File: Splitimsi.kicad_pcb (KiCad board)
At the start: 2 copper layers, 118.2 x 99.3 mm, 30 parts, among them SW1 MX_RGB, SW10 MX_RGB, SW11 MX_RGB, SW12 MX_RGB, SW13 MX_RGB, SW14 MX_RGB, SW15 MX_RGB, SW16 MX_RGB, SW17 MX_RGB, SW18 MX_RGB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

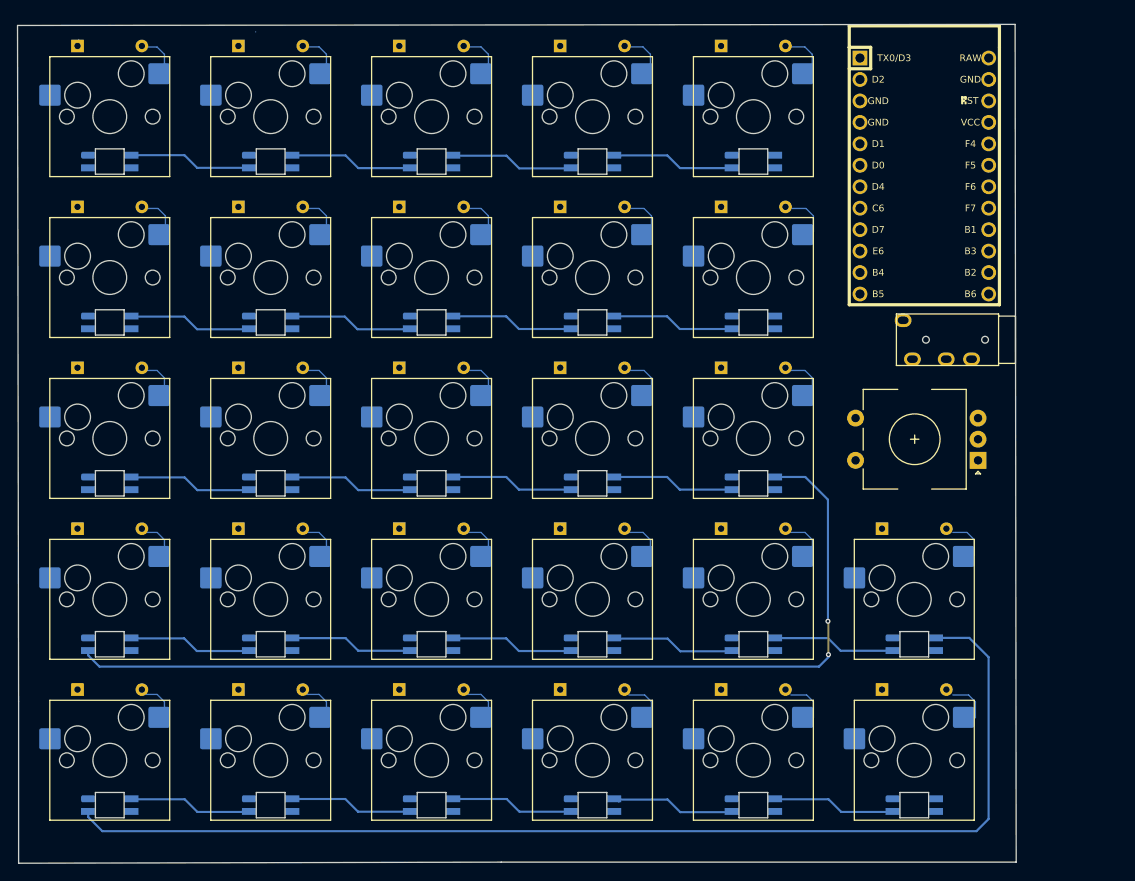
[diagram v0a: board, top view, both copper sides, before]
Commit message: tht diode footprints changed with smds
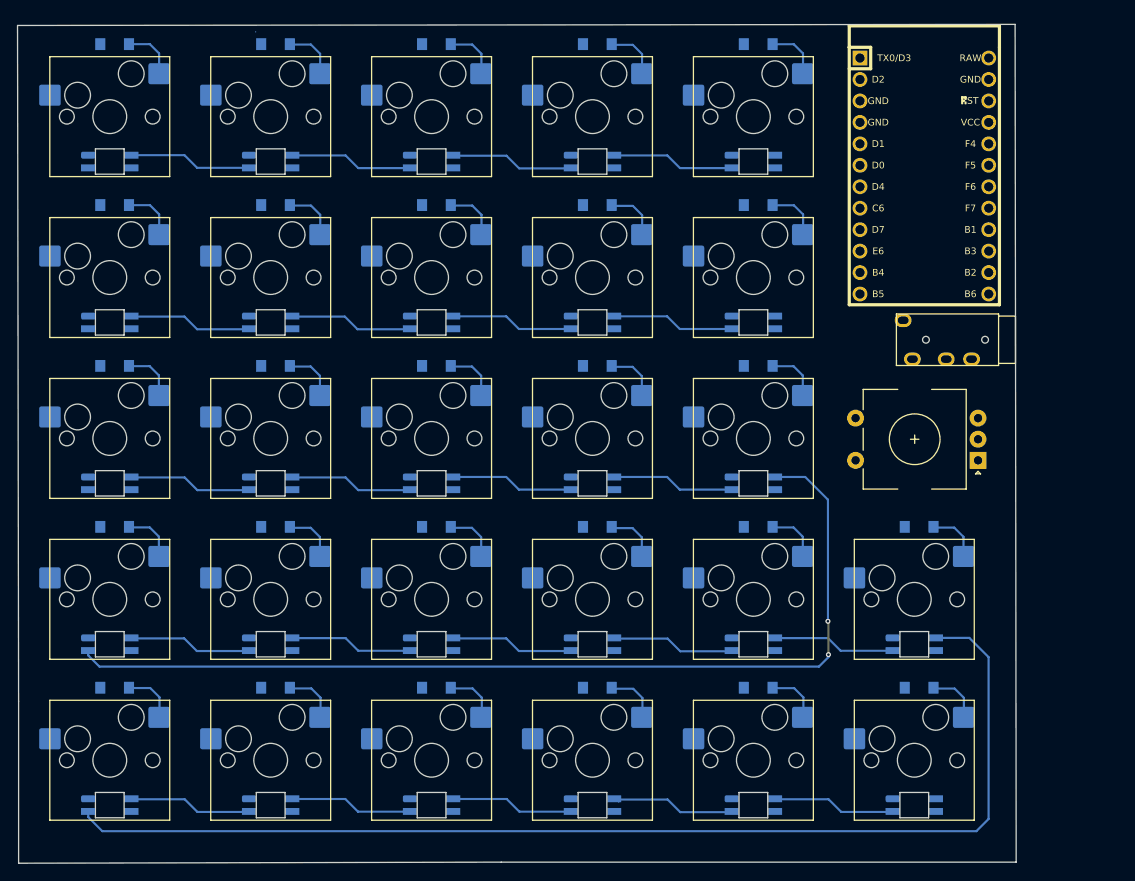
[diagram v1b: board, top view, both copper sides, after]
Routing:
- net /Row0: track 1.83 -> 0.01 mm
- net Net-(SW14-Pad2): track 4.82 -> 6.43 mm
- net Net-(SW12-Pad2): track 4.82 -> 6.43 mm
- net Net-(SW11-Pad2): track 4.82 -> 6.43 mm
- net Net-(SW9-Pad2): track 4.82 -> 6.43 mm
- net Net-(SW17-Pad2): track 4.82 -> 6.43 mm
- net Net-(SW16-Pad2): track 4.82 -> 6.43 mm
- net Net-(SW15-Pad2): track 4.82 -> 6.43 mm
- net Net-(SW20-Pad2): track 4.82 -> 6.43 mm
- net Net-(SW6-Pad2): track 4.82 -> 6.43 mm
- net Net-(SW4-Pad2): track 4.82 -> 6.43 mm
- net Net-(SW1-Pad2): track 5.54 -> 7.15 mm
- net Net-(SW7-Pad2): track 4.82 -> 6.43 mm
- net Net-(SW10-Pad2): track 4.82 -> 6.43 mm
- net Net-(SW5-Pad2): track 4.82 -> 6.43 mm
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
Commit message: Row tracks connected to the Mcu
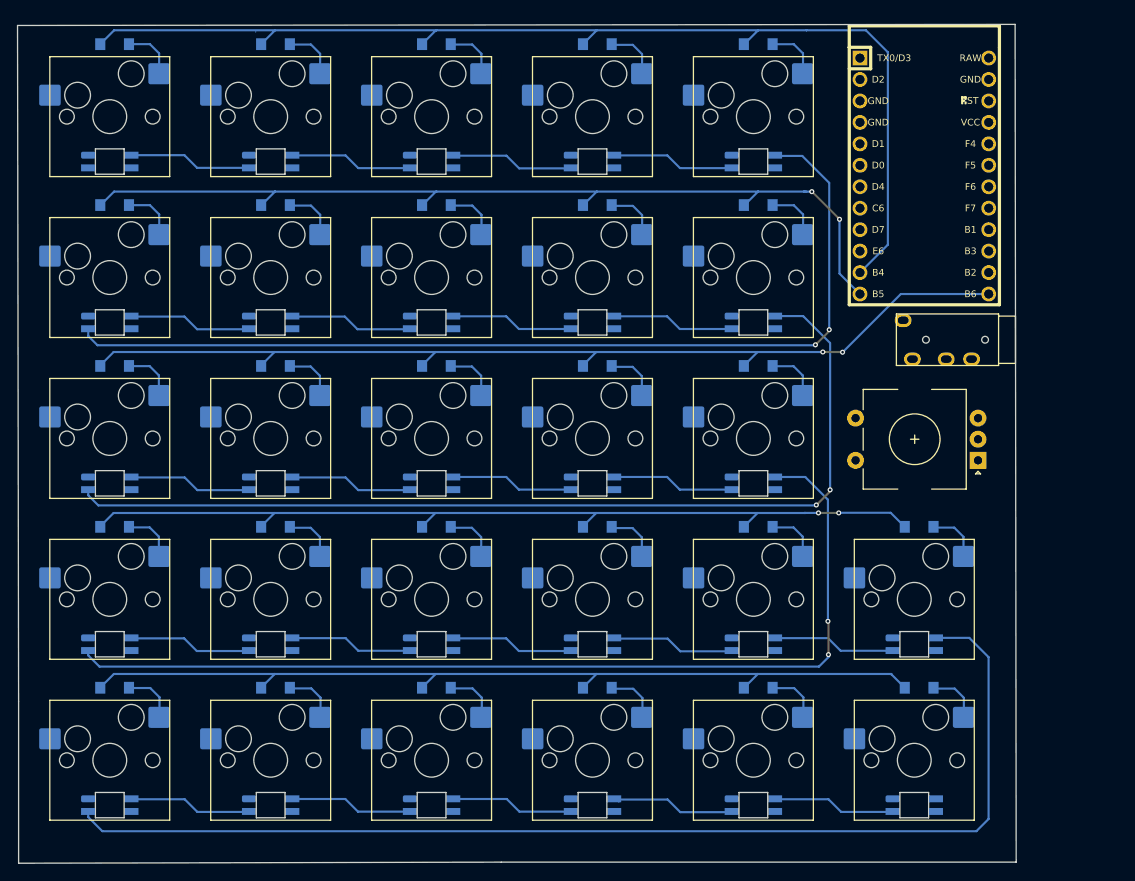
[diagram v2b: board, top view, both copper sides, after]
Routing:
- net /Row0: track 0.01 -> 131.9 mm
- net /Row2: track 0.00 -> 118.1 mm, vias 0 -> 2
- net /Row1_LedOut: track 0.00 -> 115.1 mm, vias 0 -> 2
- net /Row0_LedOut: track 0.00 -> 114.8 mm, vias 0 -> 2
- net /Row1: track 0.00 -> 109.0 mm, vias 0 -> 2
- net /Row3: track 0.00 -> 106.1 mm, vias 0 -> 2
- net /Row4: track 0.00 -> 105.9 mm

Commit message: v0.5
- rows and columns connected to the MCU
- main tracks connected except rst button, knob, gnd, trrs
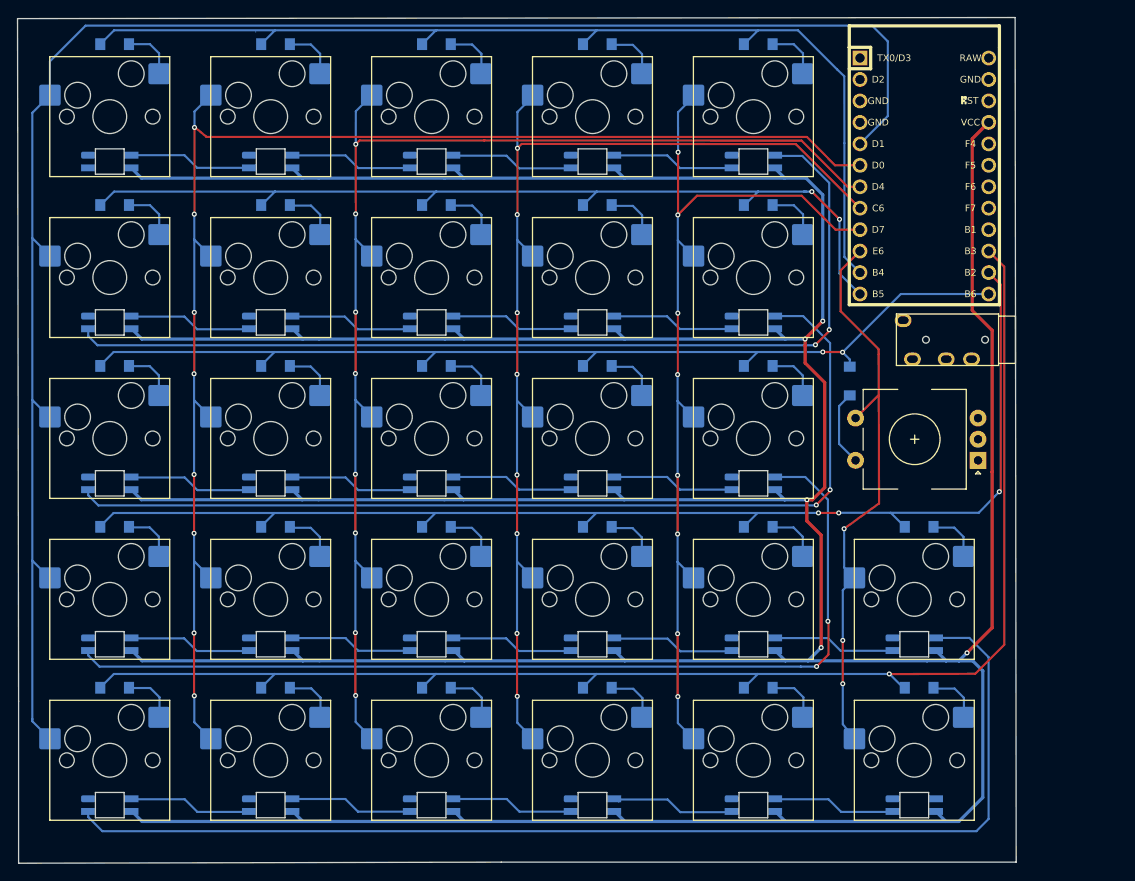
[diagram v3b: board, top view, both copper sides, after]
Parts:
- added D1: DIODE, Keebio-Parts:D_SOD123, B.Cu at (118.7, 59.9)
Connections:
- Knob1 pad S2: unconnected-(Knob1-PadS2) -> Net-(D1-Pad1)
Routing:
- net +5V: track 0.00 -> 626.6 mm, vias 0 -> 5
- net /Col0: track 0.00 -> 206.0 mm
- net /Col1: track 0.00 -> 166.7 mm, vias 0 -> 8
- net /Col2: track 0.00 -> 148.3 mm, vias 0 -> 8
- net /Col3: track 0.00 -> 130.0 mm, vias 0 -> 8
- net /Col4: track 0.00 -> 110.3 mm, vias 0 -> 8
- net /Col5: track 0.00 -> 68.0 mm, vias 0 -> 3
- net /Row4: track 105.9 -> 168.4 mm, vias 0 -> 1
- net /Row3: track 106.1 -> 146.7 mm, vias 2 -> 3
- net Net-(D1-Pad1): track 0.00 -> 9.02 mm
- net /Row0: track 131.9 -> 124.4 mm
- net /Row2: track 118.1 -> 120.1 mm
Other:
- board size 118.2 x 99.3 mm -> 118.2 x 100.1 mm

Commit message: fucked up update
- ic2 resistors added
- trrs tracks connected to the mcu
- pin 5 and 6 deleted for column tracks
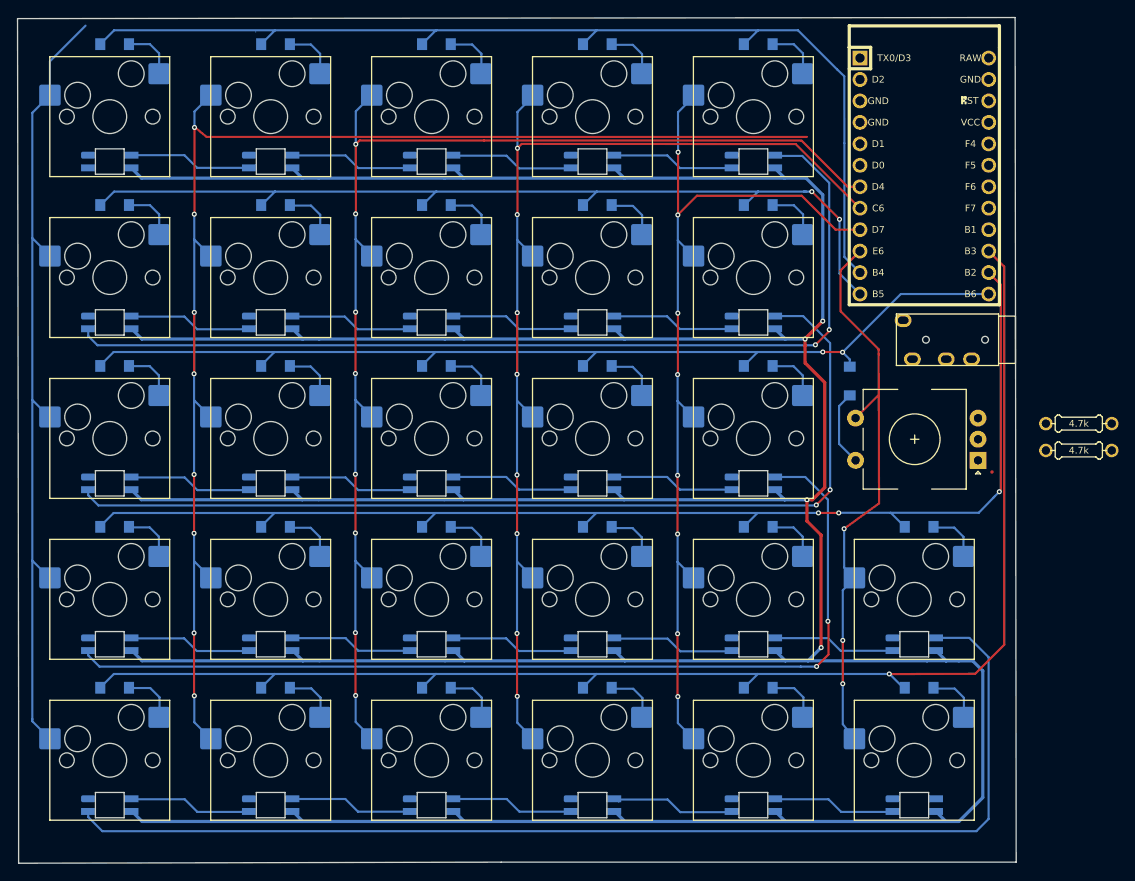
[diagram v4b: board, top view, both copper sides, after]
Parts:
- added R1: 4.7k, Keebio-Parts:Resistor-Compact-1-side, F.Cu at (145.8, 64.9)
- added R2: 4.7k, Keebio-Parts:Resistor-Compact-1-side, F.Cu at (145.8, 68.1)
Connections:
- SW1 pad 6: unconnected-(SW1-Pad6) -> /LedData
- U1 pad 1: unconnected-(U1-Pad1) -> /LedData
- U1 pad 5: /Col0 -> /SDA
- U1 pad 6: /Col1 -> /SCL
- U2 pad 1: unconnected-(U2-Pad1) -> +5V
- U2 pad 2: unconnected-(U2-Pad2) -> /SCL
- U2 pad 3: unconnected-(U2-Pad3) -> /SDA
- U2 pad 4: unconnected-(U2-Pad4) -> GND
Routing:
- net /Col0: track 206.0 -> 96.7 mm
- net +5V: track 626.6 -> 559.4 mm, vias 5 -> 4
- net /Col1: track 166.7 -> 159.1 mm

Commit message: TRRS resistors and footprints connected
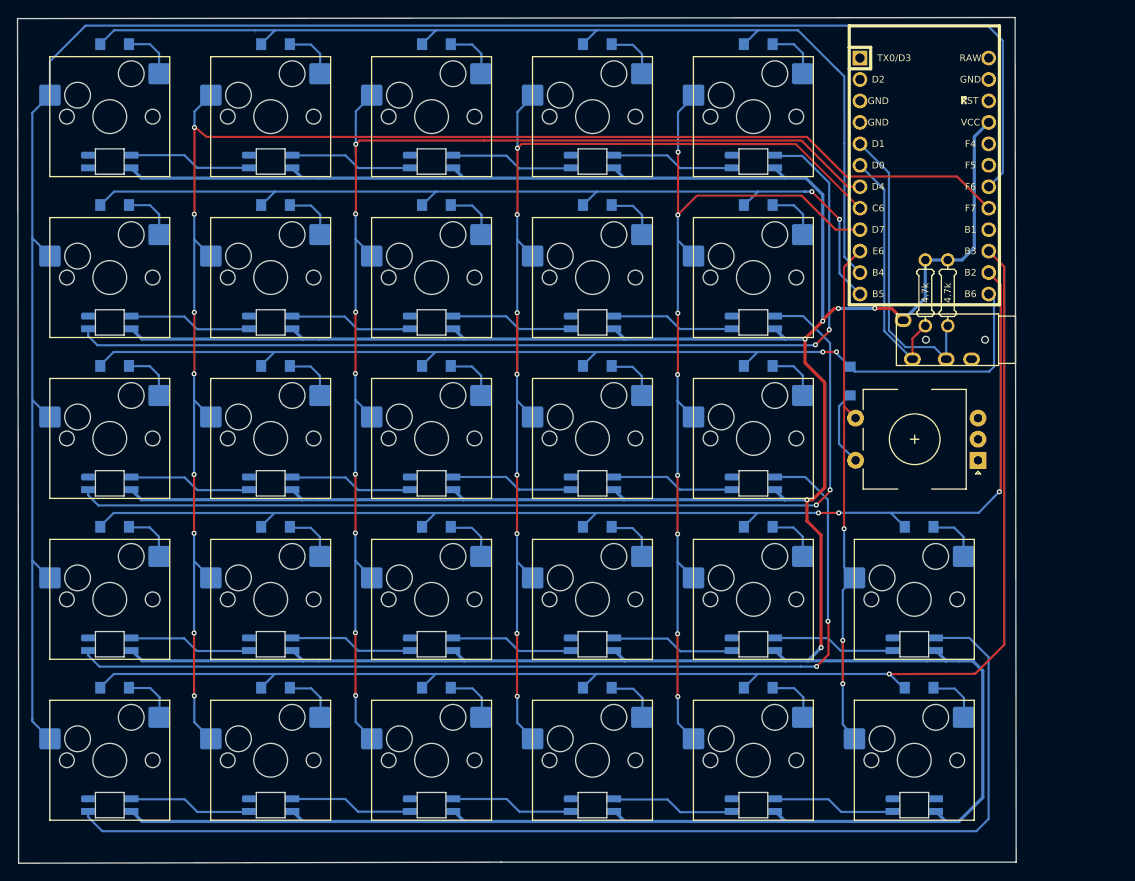
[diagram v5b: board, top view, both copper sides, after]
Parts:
- moved R2 26.0 mm to (127.7, 49.4), turned to 90 degrees
- moved R1 21.9 mm to (130.3, 49.4), turned to 90 degrees
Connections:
- U1 pad 17: unconnected-(U1-Pad17) -> /Col1
- U1 pad 18: unconnected-(U1-Pad18) -> /Col0
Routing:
- net /Col0: track 96.7 -> 224.0 mm
- net +5V: track 559.4 -> 600.4 mm, vias 4 -> 6
- net /SDA: track 0.00 -> 35.7 mm
- net /SCL: track 0.00 -> 30.1 mm
- net /Col1: track 159.1 -> 184.1 mm
- net /Col5: track 68.0 -> 62.0 mm
- net /Row2: track 120.1 -> 126.0 mm

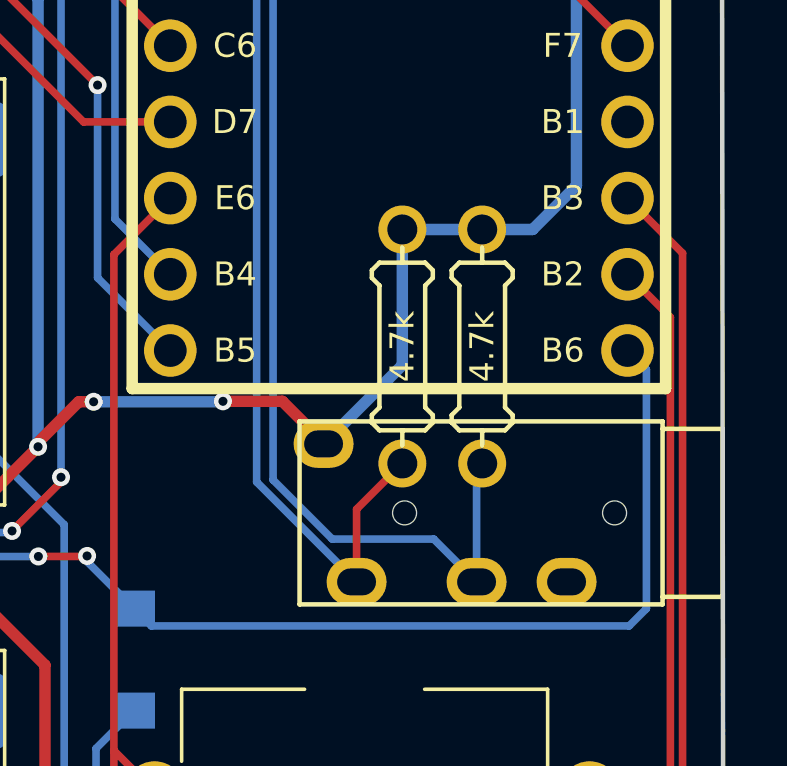
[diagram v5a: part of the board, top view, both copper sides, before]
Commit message: Resistor footprints changed with 1206
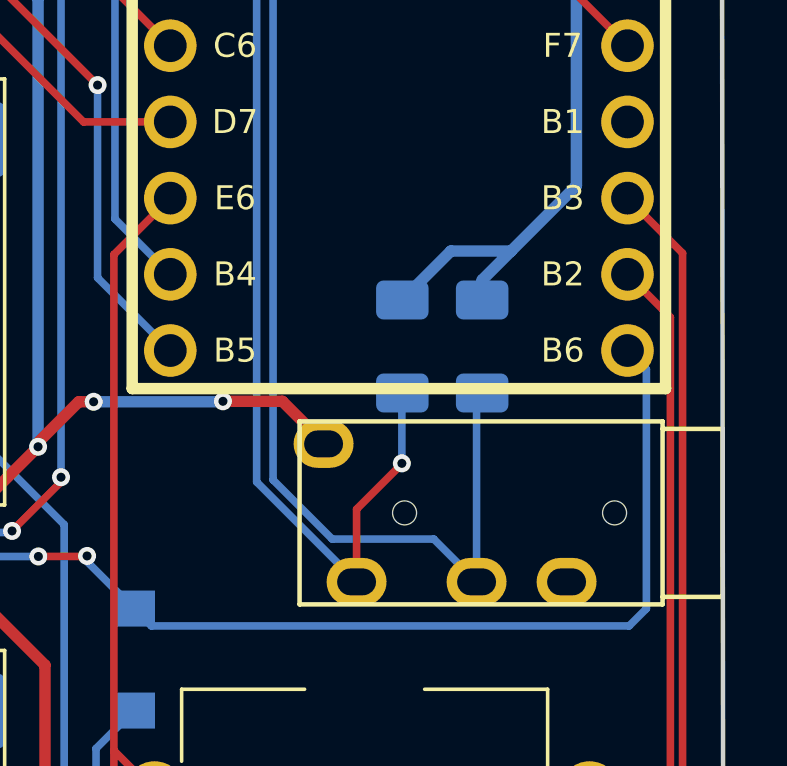
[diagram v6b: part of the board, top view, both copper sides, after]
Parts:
- R1, R2: footprint Keebio-Parts:Resistor-Compact-1-side -> Resistor_SMD:R_1206_3216Metric_Pad1.30x1.75mm_HandSolder; moved to B.Cu
- turned R1 to -90 degrees
- turned R2 to -90 degrees
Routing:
- net +5V: track 600.4 -> 595.2 mm
- net /SCL: track 30.1 -> 32.5 mm, vias 0 -> 1
- net /SDA: track 35.7 -> 38.1 mm
